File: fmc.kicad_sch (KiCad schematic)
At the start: 2 parts, among them P1 ASP-134604-01, P2 ASP-134604-01

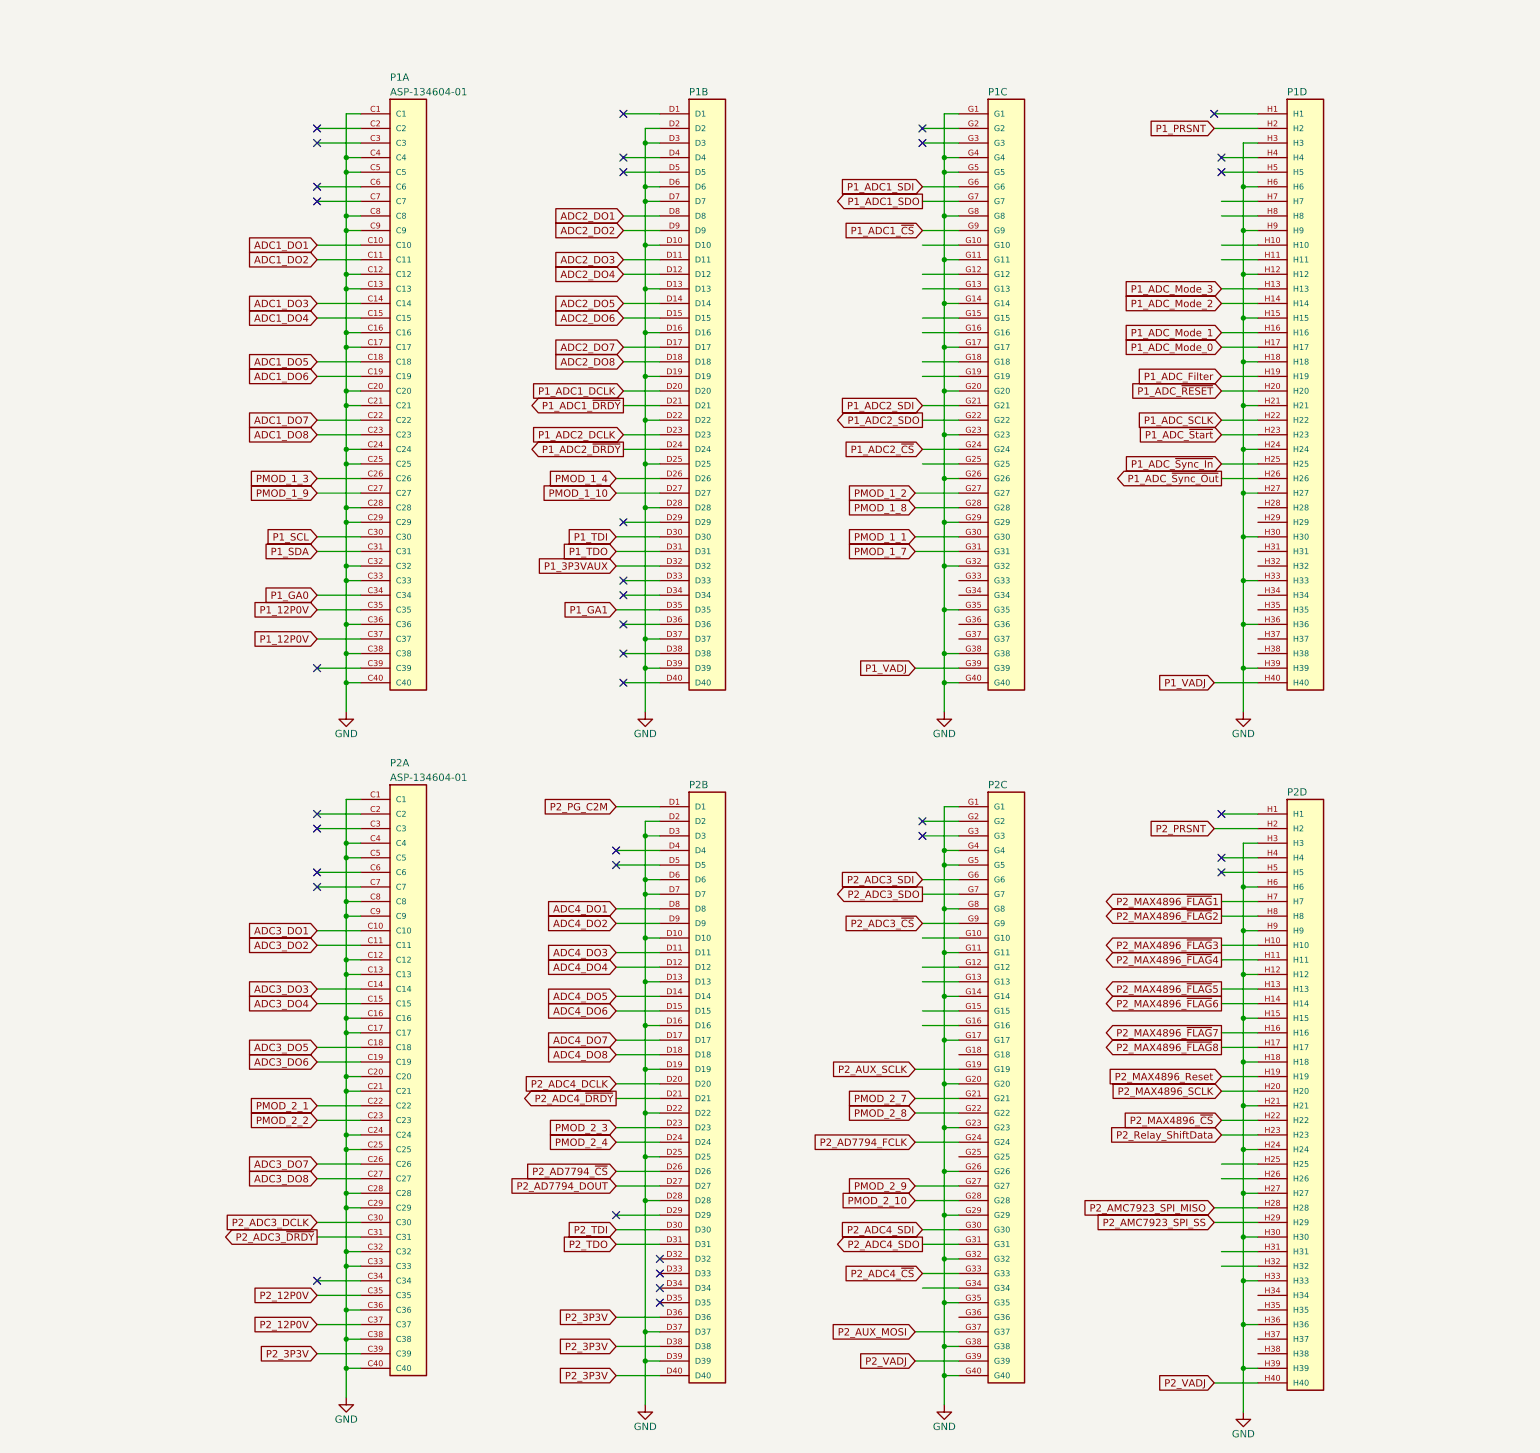
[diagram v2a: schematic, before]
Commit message: Updated Schematics with recent changes
Made Updates with recent suggestions.
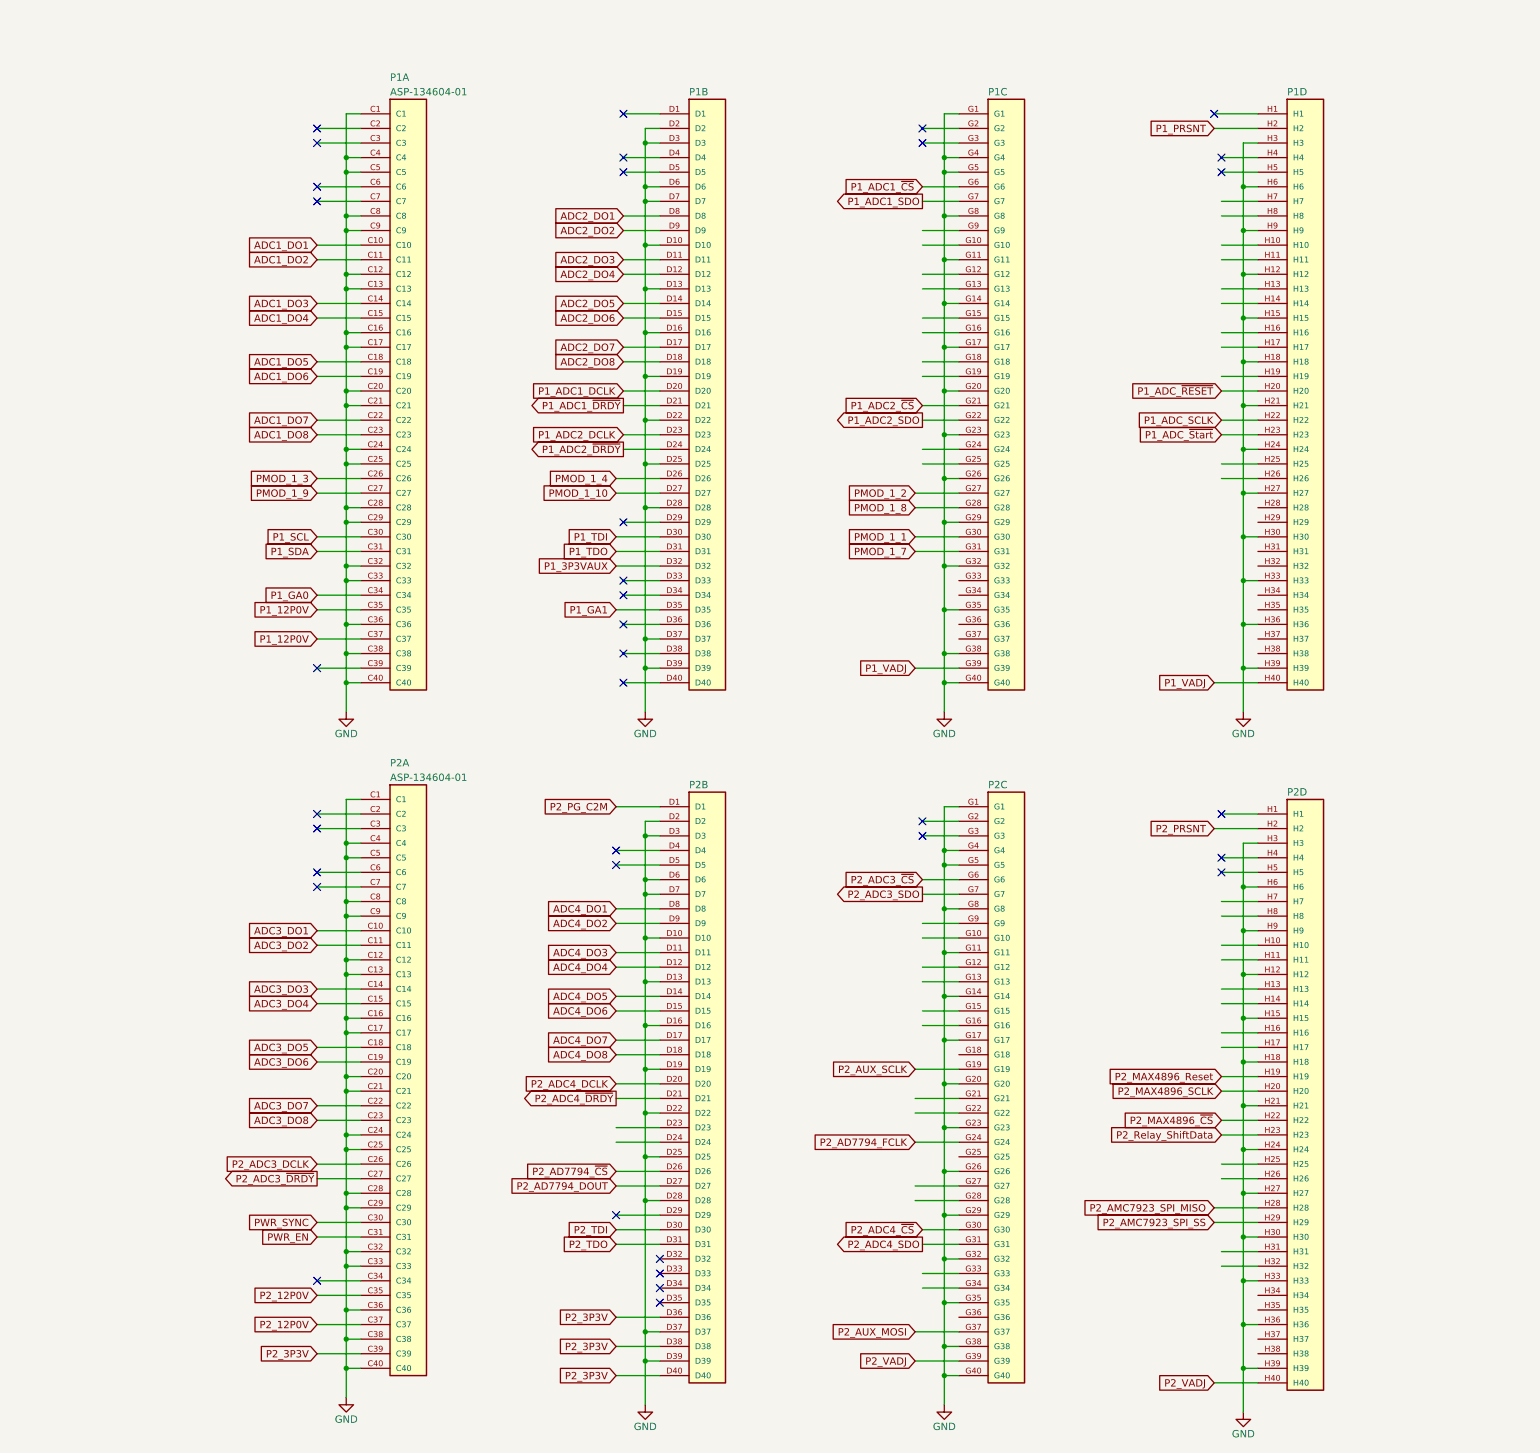
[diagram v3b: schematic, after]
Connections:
- net P1_ADC1_SDI is gone; now on net P1_ADC1_~{CS}: P1.G6
- net P1_ADC2_SDI is gone; now on net P1_ADC2_~{CS}: P1.G21
- net P2_ADC3_SDI is gone; now on net P2_ADC3_~{CS}: P2.G6
- net P2_ADC4_SDI is gone; now on net P2_ADC4_~{CS}: P2.G30
- net PMOD_2_1 is gone; now on net ADC3_DO7: P2.C22
- net PMOD_2_2 is gone; now on net ADC3_DO8: P2.C23
- net ADC3_DO7: no longer P2.C26
- net ADC3_DO8: no longer P2.C27
- net P1_ADC1_~{CS}: no longer P1.G9
- net P1_ADC2_~{CS}: no longer P1.G24
- net P2_ADC3_DCLK: now also P2.C26; no longer P2.C30
- net P2_ADC3_~{CS}: no longer P2.G9
- net P2_ADC3_~{DRDY}: now also P2.C27; no longer P2.C31
- net P2_ADC4_~{CS}: no longer P2.G33
- net P1_ADC_Filter: no longer names the net of P1.H19
- net P1_ADC_Mode_0: no longer names the net of P1.H17
- net P1_ADC_Mode_1: no longer names the net of P1.H16
- net P1_ADC_Mode_2: no longer names the net of P1.H14
- net P1_ADC_Mode_3: no longer names the net of P1.H13
- net P1_ADC_~{Sync_In}: no longer names the net of P1.H25
- net P1_ADC_~{Sync_Out}: no longer names the net of P1.H26
- net P2_MAX4896_~{FLAG}1: no longer names the net of P2.H7
- net P2_MAX4896_~{FLAG}2: no longer names the net of P2.H8
- net P2_MAX4896_~{FLAG}3: no longer names the net of P2.H10
- net P2_MAX4896_~{FLAG}4: no longer names the net of P2.H11
- net P2_MAX4896_~{FLAG}5: no longer names the net of P2.H13
- net P2_MAX4896_~{FLAG}6: no longer names the net of P2.H14
- net P2_MAX4896_~{FLAG}7: no longer names the net of P2.H16
- net P2_MAX4896_~{FLAG}8: no longer names the net of P2.H17
- net PMOD_2_10: no longer names the net of P2.G28
- net PMOD_2_3: no longer names the net of P2.D23
- net PMOD_2_4: no longer names the net of P2.D24
- net PMOD_2_7: no longer names the net of P2.G21
- net PMOD_2_8: no longer names the net of P2.G22
- net PMOD_2_9: no longer names the net of P2.G27
- new net PWR_EN: P2.C31
- new net PWR_SYNC: P2.C30

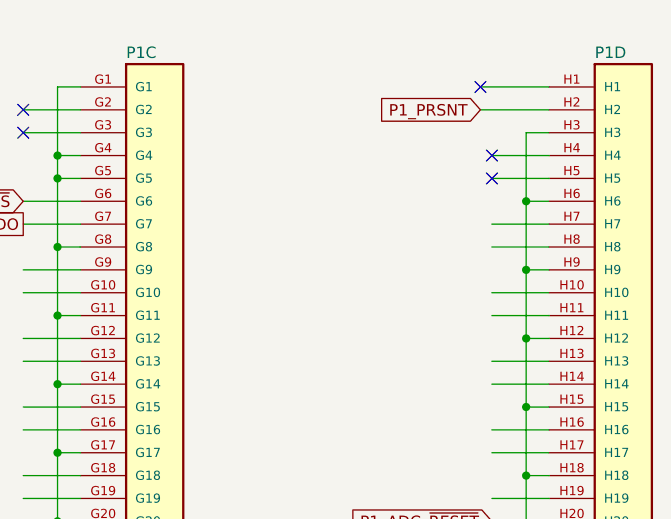
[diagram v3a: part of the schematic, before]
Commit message: Updated Channel 1 and fixes from review
Updated Channel 1 to use the INA851.
Fixed the ORNTA part pinout.
Fixed feedback on LT1763s.
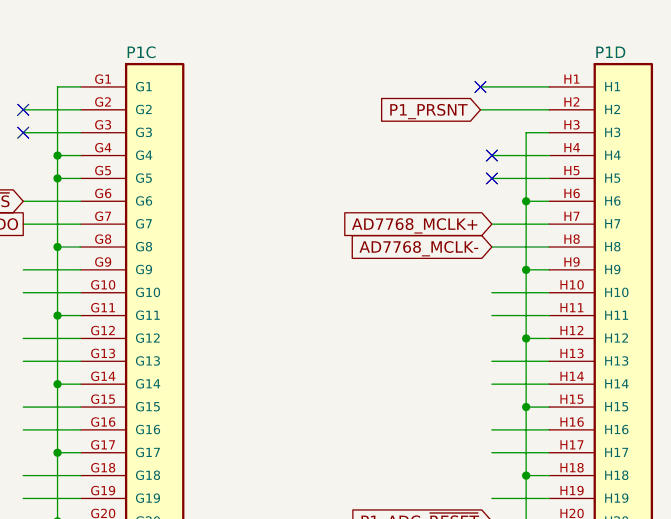
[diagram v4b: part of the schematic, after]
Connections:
- net AD7768_MCLK+: now reaches P1.H7
- net AD7768_MCLK-: now reaches P1.H8
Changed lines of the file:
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@@
+    )
+  )
+  (global_label "AD7768_MCLK-" (shape input) (at 275.59 49.53 180) (fields_autoplaced)
+    (effects (font (size 1.27 1.27)) (justify right))
+    (property "Intersheetrefs" "${INTERSHEET_REFS}" (at 257.8487 49.53 0)
+      (effects (font (size 1.27 1.27)) (justify right) hide)
     )
   )
@@
       (effects (font (size 1.27 1.27)) (justify right) hide)
     )
+  )
+  (global_label "AD7768_MCLK+" (shape input) (at 275.59 46.99 180) (fields_autoplaced)
+    (effects (font (size 1.27 1.27)) (justify right))
+    (property "Intersheetrefs" "${INTERSHEET_REFS}" (at 257.8487 46.99 0)
+      (effects (font (size 1.27 1.27)) (justify right) hide)
+    )
